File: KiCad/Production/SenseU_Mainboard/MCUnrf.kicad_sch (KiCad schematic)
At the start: 5 parts

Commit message: added USB TO UART
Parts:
- added C19, C20: C, symbol Device:C
- added U4: COM-16278, SOP50P490X120-10N, symbol CH340:COM-16278
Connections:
- net DATA+: now also U4.1 (UD+)
- net DATA-: now also U4.2 (UD-)
- net GND: now also C19.2, C20.2, U4.3 (GND)
- net VBUS: now also C19.1, U4.7 (VCC)
- new net: C20.1, U4.10 (V3)
- new net UART_NCTS: U4.5 (~{CTS})
- new net UART_NRTS: U4.4 (~{RTS})
- new net UART_RX: U4.9 (RXD)
- new net UART_TX: U4.8 (TXD)
- no-connect marks 1 -> 3
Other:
- sheet FPGA ports: added UART_NCTS, UART_NRTS; removed none

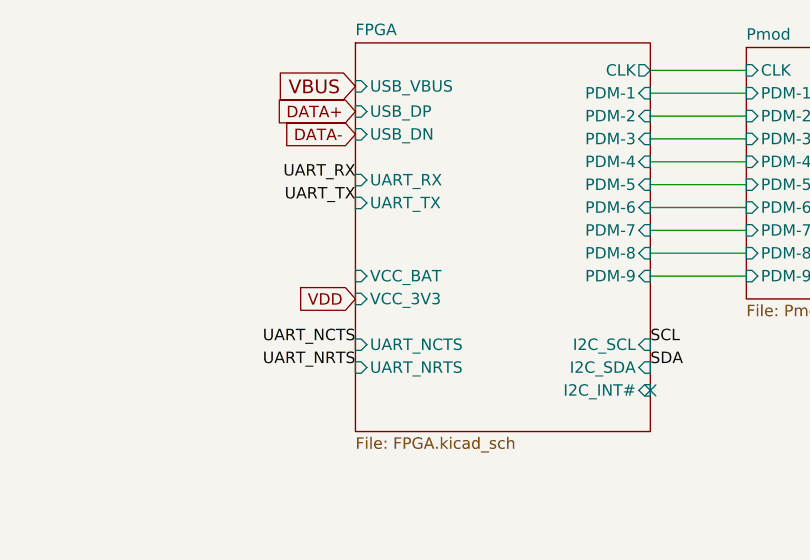
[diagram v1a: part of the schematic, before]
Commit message: removed batt co to fpga and added switch
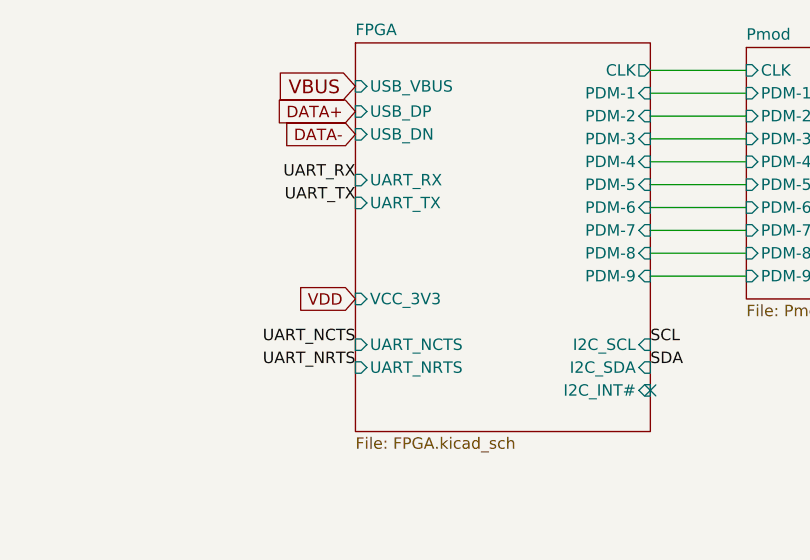
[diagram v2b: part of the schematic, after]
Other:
- sheet FPGA ports: added none; removed VCC_BAT
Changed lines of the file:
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@@
       (effects (font (size 1.27 1.27)) (justify right))
-    )
-    (pin "VCC_BAT" input (at 105.156 55.88 180)
-      (effects (font (size 1.27 1.27)) (justify left))
     )
     (pin "I2C_SCL" input (at 137.922 63.5 0)

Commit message: changed place of usb to uart
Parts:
- C19, C20: footprint (none) -> Capacitor_SMD:C_0603_1608Metric_Pad1.08x0.95mm_HandSolder
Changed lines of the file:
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@@
       (effects (font (size 1.27 1.27)) (justify left))
     )
-    (property "Footprint" "" (at 256.2352 50.292 0)
+    (property "Footprint" "Capacitor_SMD:C_0603_1608Metric_Pad1.08x0.95mm_HandSolder" (at 256.2352 50.292 0)
       (effects (font (size 1.27 1.27)) hide)
     )
@@
       (effects (font (size 1.27 1.27)) (justify left))
     )
-    (property "Footprint" "" (at 266.3952 47.752 0)
+    (property "Footprint" "Capacitor_SMD:C_0603_1608Metric_Pad1.08x0.95mm_HandSolder" (at 266.3952 47.752 0)
       (effects (font (size 1.27 1.27)) hide)
     )

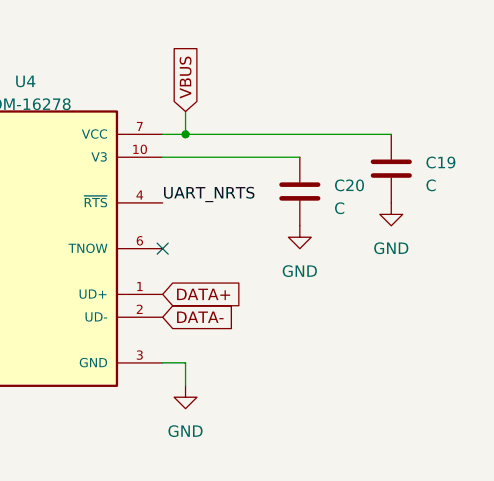
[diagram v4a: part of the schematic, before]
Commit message: routing SenseU done
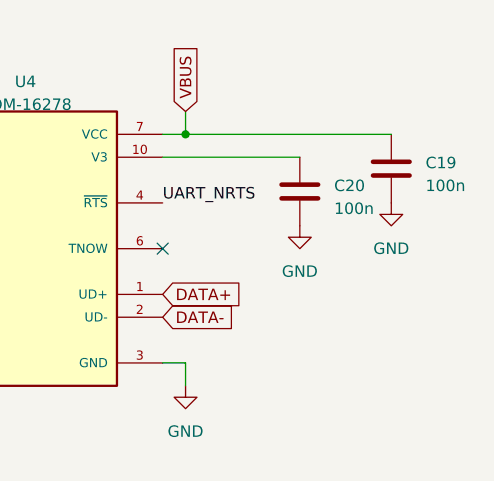
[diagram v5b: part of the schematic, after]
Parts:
- C19, C20: value C -> 100n; footprint Capacitor_SMD:C_0603_1608Metric_Pad1.08x0.95mm_HandSolder -> Capacitor_SMD:C_0603_1608Metric
- U4: footprint SOP50P490X120-10N -> CH340:SOP50P490X120-10N
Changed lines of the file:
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@@
     (instances
       (project "SenseU_Mainboard"
-        (path "/43872b54-cf9c-4c7b-870d-631baccef0c0/d8d785fb-fd90-4cd9-a47e-213577f6aaa3"
-          (reference "#PWR073") (unit 1)
-        )
         (path "/43872b54-cf9c-4c7b-870d-631baccef0c0/915563dd-e56c-42ce-a954-58d654408565"
           (reference "#PWR015") (unit 1)
@@
       (effects (font (size 1.27 1.27)) (justify left))
     )
-    (property "Value" "C" (at 259.08 48.387 0)
-      (effects (font (size 1.27 1.27)) (justify left))
-    )
-    (property "Footprint" "Capacitor_SMD:C_0603_1608Metric_Pad1.08x0.95mm_HandSolder" (at 256.2352 50.292 0)
+    (property "Value" "100n" (at 259.08 48.387 0)
+      (effects (font (size 1.27 1.27)) (justify left))
+    )
+    (property "Footprint" "Capacitor_SMD:C_0603_1608Metric" (at 256.2352 50.292 0)
       (effects (font (size 1.27 1.27)) hide)
     )
@@
     (instances
       (project "SenseU_Mainboard"
-        (path "/43872b54-cf9c-4c7b-870d-631baccef0c0/d8d785fb-fd90-4cd9-a47e-213577f6aaa3"
-          (reference "C20") (unit 1)
-        )
         (path "/43872b54-cf9c-4c7b-870d-631baccef0c0/915563dd-e56c-42ce-a954-58d654408565"
           (reference "C5") (unit 1)
@@
       (effects (font (size 1.27 1.27)) (justify left))
     )
-    (property "Value" "C" (at 269.24 45.847 0)
-      (effects (font (size 1.27 1.27)) (justify left))
-    )
-    (property "Footprint" "Capacitor_SMD:C_0603_1608Metric_Pad1.08x0.95mm_HandSolder" (at 266.3952 47.752 0)
+    (property "Value" "100n" (at 269.24 45.847 0)
+      (effects (font (size 1.27 1.27)) (justify left))
+    )
+    (property "Footprint" "Capacitor_SMD:C_0603_1608Metric" (at 266.3952 47.752 0)
       (effects (font (size 1.27 1.27)) hide)
     )
@@
     (instances
       (project "SenseU_Mainboard"
-        (path "/43872b54-cf9c-4c7b-870d-631baccef0c0/d8d785fb-fd90-4cd9-a47e-213577f6aaa3"
-          (reference "C19") (unit 1)
-        )
         (path "/43872b54-cf9c-4c7b-870d-631baccef0c0/915563dd-e56c-42ce-a954-58d654408565"
           (reference "C6") (unit 1)
@@
     (instances
       (project "SenseU_Mainboard"
-        (path "/43872b54-cf9c-4c7b-870d-631baccef0c0/d8d785fb-fd90-4cd9-a47e-213577f6aaa3"
-          (reference "#PWR071") (unit 1)
-        )
         (path "/43872b54-cf9c-4c7b-870d-631baccef0c0/915563dd-e56c-42ce-a954-58d654408565"
           (reference "#PWR017") (unit 1)
@@
       (effects (font (size 1.27 1.27)))
     )
-    (property "Footprint" "SOP50P490X120-10N" (at 224.79 52.832 0)
+    (property "Footprint" "CH340:SOP50P490X120-10N" (at 224.79 52.832 0)
       (effects (font (size 1.27 1.27)) (justify bottom) hide)
     )
@@
     (instances
       (project "SenseU_Mainboard"
-        (path "/43872b54-cf9c-4c7b-870d-631baccef0c0/d8d785fb-fd90-4cd9-a47e-213577f6aaa3"
-          (reference "U4") (unit 1)
-        )
         (path "/43872b54-cf9c-4c7b-870d-631baccef0c0/915563dd-e56c-42ce-a954-58d654408565"
           (reference "U3") (unit 1)
@@
     (instances
       (project "SenseU_Mainboard"
-        (path "/43872b54-cf9c-4c7b-870d-631baccef0c0/d8d785fb-fd90-4cd9-a47e-213577f6aaa3"
-          (reference "#PWR072") (unit 1)
-        )
         (path "/43872b54-cf9c-4c7b-870d-631baccef0c0/915563dd-e56c-42ce-a954-58d654408565"
           (reference "#PWR016") (unit 1)
